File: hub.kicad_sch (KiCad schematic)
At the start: 58 parts, among them J1 USB3_A_LCSC, J2 USB3_A_LCSC, J5 USB3_A_LCSC, J6 USB3_A_LCSC, J7 USB3_A_LCSC, J8 USB3_A_LCSC, U10 TPD1E05U06DPY, U12 TPD1E05U06DPY, U13 TPD1E05U06DPY, U2 TPD1E05U06DPY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

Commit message: Add PI3DPX1203BZLEX DisplayPort redriver and start adding it to schematic
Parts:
- C37, C38, C39, C40, C41, C42, C43, C44: footprint Capacitor_SMD:C_0603_1608Metric -> Capacitor_SMD:C_0402_1005Metric
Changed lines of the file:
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@@
 			)
 		)
-		(property "Footprint" "Capacitor_SMD:C_0603_1608Metric"
+		(property "Footprint" "Capacitor_SMD:C_0402_1005Metric"
 			(at 306.07 104.14 0)
 			(effects
@@
 			)
 		)
-		(property "Footprint" "Capacitor_SMD:C_0603_1608Metric"
+		(property "Footprint" "Capacitor_SMD:C_0402_1005Metric"
 			(at 306.07 139.7 0)
 			(effects
@@
 			)
 		)
-		(property "Footprint" "Capacitor_SMD:C_0603_1608Metric"
+		(property "Footprint" "Capacitor_SMD:C_0402_1005Metric"
 			(at 297.18 119.38 0)
 			(effects
@@
 			)
 		)
-		(property "Footprint" "Capacitor_SMD:C_0603_1608Metric"
+		(property "Footprint" "Capacitor_SMD:C_0402_1005Metric"
 			(at 306.07 157.48 0)
 			(effects
@@
 			)
 		)
-		(property "Footprint" "Capacitor_SMD:C_0603_1608Metric"
+		(property "Footprint" "Capacitor_SMD:C_0402_1005Metric"
 			(at 297.18 101.6 0)
 			(effects
@@
 			)
 		)
-		(property "Footprint" "Capacitor_SMD:C_0603_1608Metric"
+		(property "Footprint" "Capacitor_SMD:C_0402_1005Metric"
 			(at 306.07 121.92 0)
 			(effects
@@
 			)
 		)
-		(property "Footprint" "Capacitor_SMD:C_0603_1608Metric"
+		(property "Footprint" "Capacitor_SMD:C_0402_1005Metric"
 			(at 297.18 154.94 0)
 			(effects
@@
 			)
 		)
-		(property "Footprint" "Capacitor_SMD:C_0603_1608Metric"
+		(property "Footprint" "Capacitor_SMD:C_0402_1005Metric"
 			(at 297.18 137.16 0)
 			(effects

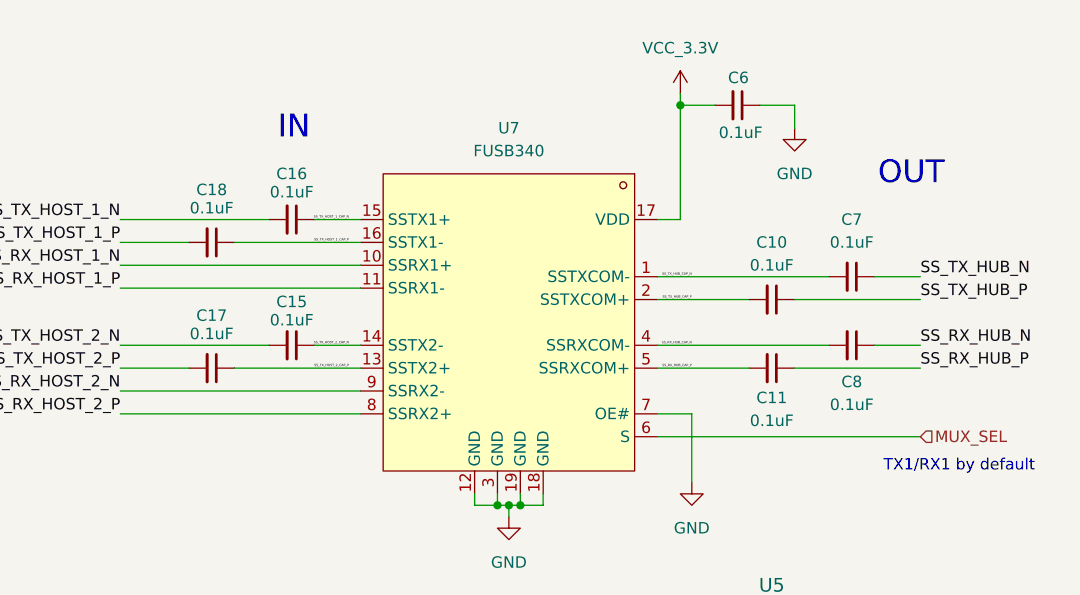
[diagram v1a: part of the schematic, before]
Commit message: Change all high-speed decoupling caps to 0402s
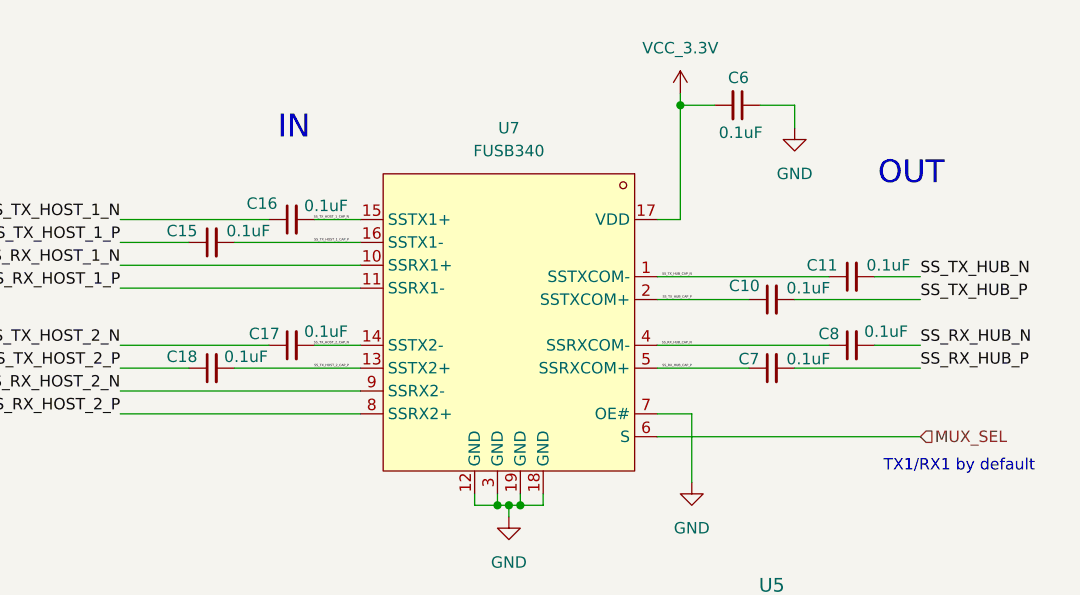
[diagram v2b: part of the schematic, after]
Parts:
- C10, C11, C15, C16, C17, C18, C7, C8: footprint Capacitor_SMD:C_0603_1608Metric -> Capacitor_SMD:C_0402_1005Metric
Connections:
- net SS_RX_HUB_CAP_N: now also C8.1; no longer C8.2
- net SS_RX_HUB_CAP_P: now also C7.1; no longer C11.2
- net SS_RX_HUB_N: now also C8.2; no longer C8.1
- net SS_RX_HUB_P: now also C7.2; no longer C11.1
- net SS_TX_HOST_1_CAP_N: now also C16.2; no longer C16.1
- net SS_TX_HOST_1_CAP_P: now also C15.2; no longer C18.1
- net SS_TX_HOST_1_N: now also C16.1; no longer C16.2
- net SS_TX_HOST_1_P: now also C15.1; no longer C18.2
- net SS_TX_HOST_2_CAP_N: now also C17.2; no longer C15.1
- net SS_TX_HOST_2_CAP_P: now also C18.2; no longer C17.1
- net SS_TX_HOST_2_N: now also C17.1; no longer C15.2
- net SS_TX_HOST_2_P: now also C18.1; no longer C17.2
- net SS_TX_HUB_CAP_N: now also C11.1; no longer C7.2
- net SS_TX_HUB_CAP_P: now also C10.1; no longer C10.2
- net SS_TX_HUB_N: now also C11.2; no longer C7.1
- net SS_TX_HUB_P: now also C10.2; no longer C10.1
